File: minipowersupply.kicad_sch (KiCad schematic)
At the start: 43 parts, among them J1 Conn_01x08_Female, J2 Conn_01x08_Female, J3 Conn_01x03_Female, J4 Conn_01x08_Female, J5 Conn_01x03_Female, J6 Conn_01x08_Female, J7 Conn_01x03_Female, J8 Conn_01x02_Female, J9 Conn_01x02_Female, Q1 BC817, U1 LM7805_TO220, U15 LT1084-3.3, U2 LM317L_TO92, U3 LM337L_TO92, U4 CD74HC4067SM

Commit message: finalising diagram
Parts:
- removed A1: Arduino_Nano_v2.x, Module:Arduino_Nano, symbol MCU_Module:Arduino_Nano_v2.x
- removed C1, C2: 150uF, Capacitor_THT:CP_Radial_D8.0mm_P3.50mm, symbol minipowersupply-rescue:CP-Device
- removed C3, C4, C5, C6, C8: 100nF, Capacitor_THT:C_Disc_D8.0mm_W5.0mm_P5.00mm, symbol Device:C
- removed C7, C9: 1uF, Capacitor_THT:C_Disc_D8.0mm_W5.0mm_P5.00mm, symbol Device:C_Polarized_Small
- removed D1, D2, D3, D4, D5, D6: D, Diode_THT:D_T-1_P10.16mm_Horizontal, symbol Device:D
- removed F1: Fuse, Fuse:Fuseholder_Cylinder-5x20mm_Bulgin_FX0457_Horizontal_Closed, symbol Device:Fuse
- removed J1, J2, J4, J6: Conn_01x08_Female, Connector_PinHeader_2.54mm:PinHeader_1x08_P2.54mm_Vertical, symbol Connector:Conn_01x08_Female
- removed J3, J5, J7: Conn_01x03_Female, Connector_PinHeader_2.54mm:PinHeader_1x03_P2.54mm_Vertical, symbol Connector:Conn_01x03_Female
- removed J8, J9: Conn_01x02_Female, Connector_PinHeader_2.54mm:PinHeader_1x02_P2.54mm_Vertical, symbol Connector:Conn_01x02_Female
- removed Q1: BC817, Package_TO_SOT_SMD:SOT-23, symbol Transistor_BJT:BC817
- removed R1: 410, Resistor_THT:R_Axial_DIN0207_L6.3mm_D2.5mm_P5.08mm_Vertical, symbol Device:R_Small
- removed R2: 4.420k, Resistor_THT:R_Axial_DIN0207_L6.3mm_D2.5mm_P5.08mm_Vertical, symbol Device:R_Small
- removed R3: 698, Resistor_THT:R_Axial_DIN0207_L6.3mm_D2.5mm_P5.08mm_Vertical, symbol Device:R_Small
- removed R4, R5: 240, Resistor_THT:R_Axial_DIN0207_L6.3mm_D2.5mm_P5.08mm_Vertical, symbol Device:R_Small
- removed RV1, RV2: 5k, symbol minipowersupply-rescue:R_POT_Small-Device
- removed TP1, TP2, TP3: TestPoint, TestPoint:TestPoint_THTPad_4.0x4.0mm_Drill2.0mm, symbol Connector:TestPoint
- removed TR1: TRANSF3, minipowersupply:vtxtfr, symbol Transformer:TRANSF3
- removed U1: LM7805_TO220, Package_TO_SOT_SMD:SOT-223-3_TabPin2, symbol Regulator_Linear:LM7805_TO220
- removed U15: LT1084-3.3, symbol Regulator_Linear:LT1084-3.3
- removed U2: LM317L_TO92, Package_TO_SOT_THT:TO-92_Inline, symbol Regulator_Linear:LM317L_TO92
- removed U3: LM337L_TO92, Package_TO_SOT_THT:TO-92_Inline, symbol Regulator_Linear:LM337L_TO92
- removed U4: CD74HC4067SM, Package_SO:SSOP-24_5.3x8.2mm_P0.65mm, symbol 74xx:CD74HC4067SM
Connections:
- no-connect marks 31 -> 1
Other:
- removed sheet Curent and Volt4
- removed sheet Curent and Volt5
- removed sheet Curent and Volt6
- removed sheet Curent and Volt7
- removed sheet Curent and Volt8
- added sheet  Measure and Mux (arduino.kicad_sch)
- added sheet Clock and TTL (CKTTL.kicad_sch)
- added sheet DualAdj (dualadj.kicad_sch)
- added sheet Measure and Control (MAC.kicad_sch)
- added sheet Unregulated Power (untitled.kicad_sch)
- note removed: "Adjustable Dual Regulated Supply"
- note removed: "Clock Pulse Generator"
- note removed: "Dual Adjustable Regulated Supply"
- note removed: "Low Voltage"
- note removed: "Mains"
- note removed: "Outputs"
- note removed: "Regulated Power"
- note removed: "Regulated TTL and 100Hz CK"
- note removed: "Unregulated Dual Supply"
- note removed: "Unregulated Power"

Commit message: last TH mounting board
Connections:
- no-connect marks 1 -> 0
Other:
- sheet Measure and Control ports: added GND; removed none
- sheet Unregulated Power: file untitled.kicad_sch -> Unregpower.kicad_sch

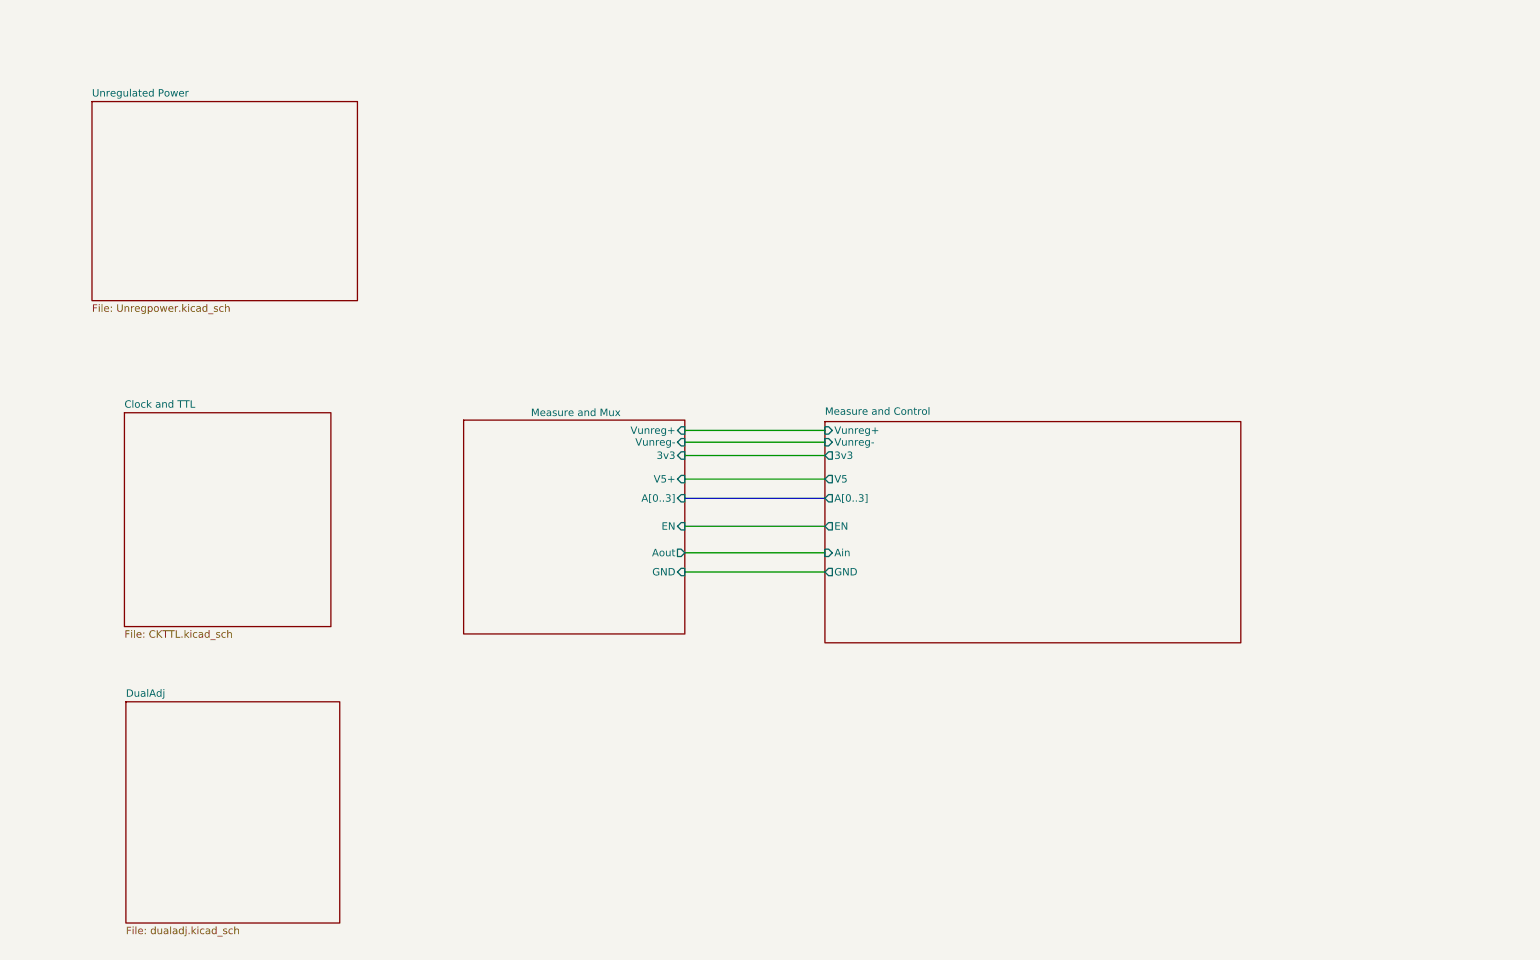
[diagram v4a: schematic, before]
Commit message: new board with SMD
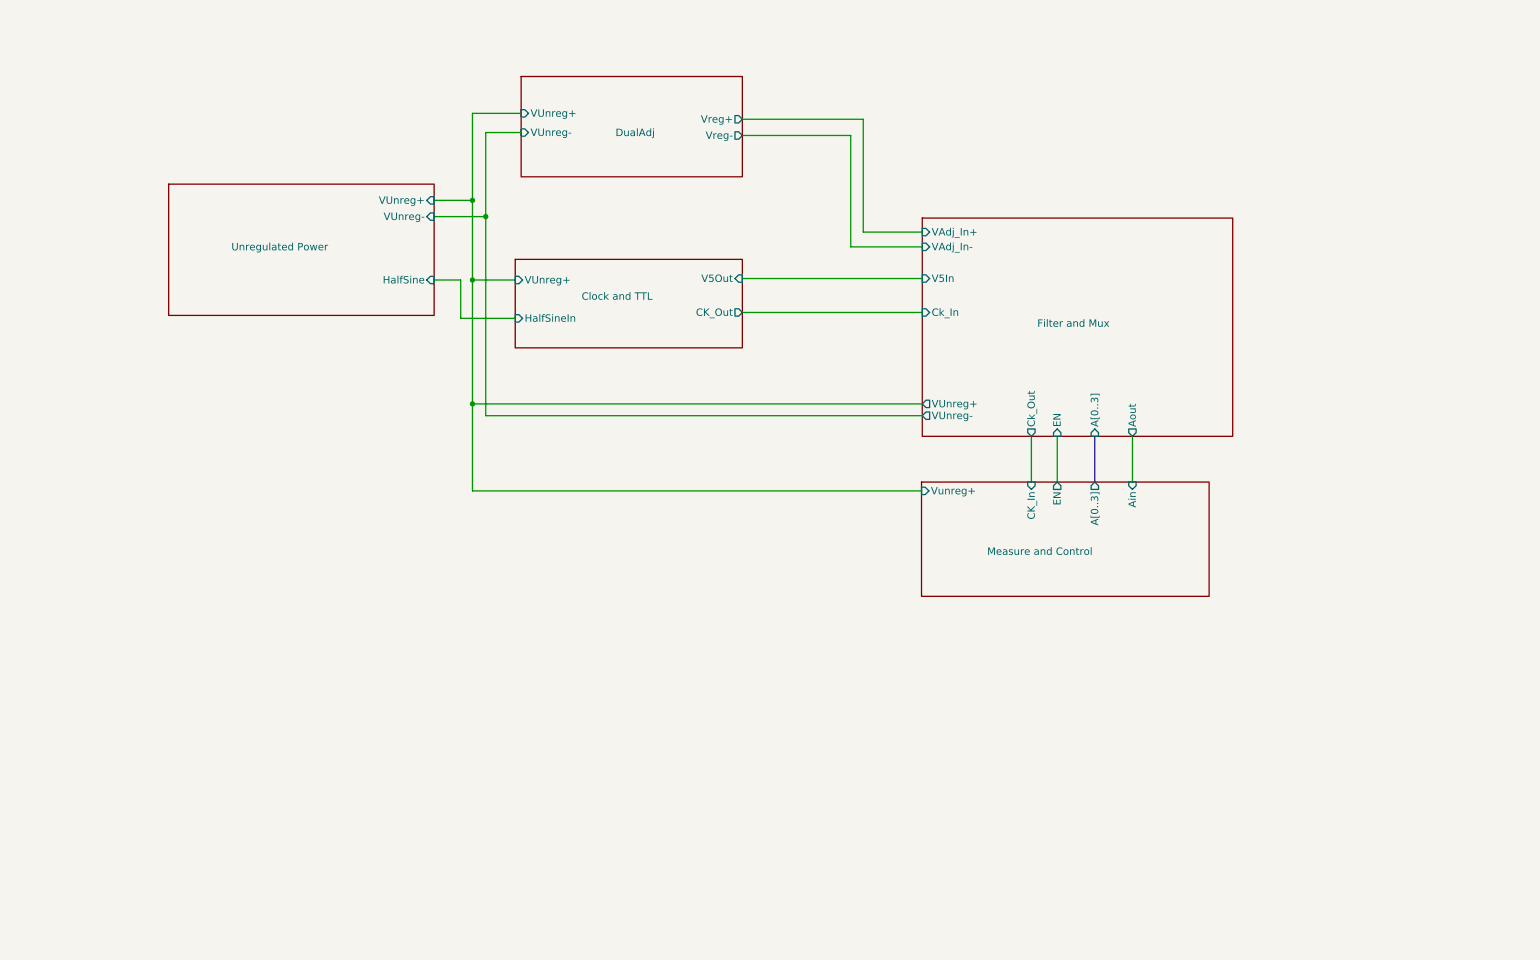
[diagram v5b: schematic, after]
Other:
- sheet  Measure and Mux renamed Filter and Mux
- sheet Clock and TTL ports: added CK_Out, HalfSineIn, V5Out, VUnreg+; removed none
- sheet DualAdj ports: added VUnreg+, VUnreg-, Vreg+, Vreg-; removed none
- sheet Filter and Mux ports: added Ck_In, Ck_Out, V5In, VAdj_In+, VAdj_In-, VUnreg+, VUnreg-; removed 3v3, GND, V5+, Vunreg+, Vunreg-
- sheet Measure and Control ports: added CK_In; removed 3v3, GND, V5, Vunreg-
- sheet Unregulated Power ports: added HalfSine, VUnreg+, VUnreg-; removed none

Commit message: New single board with all SMD in progress
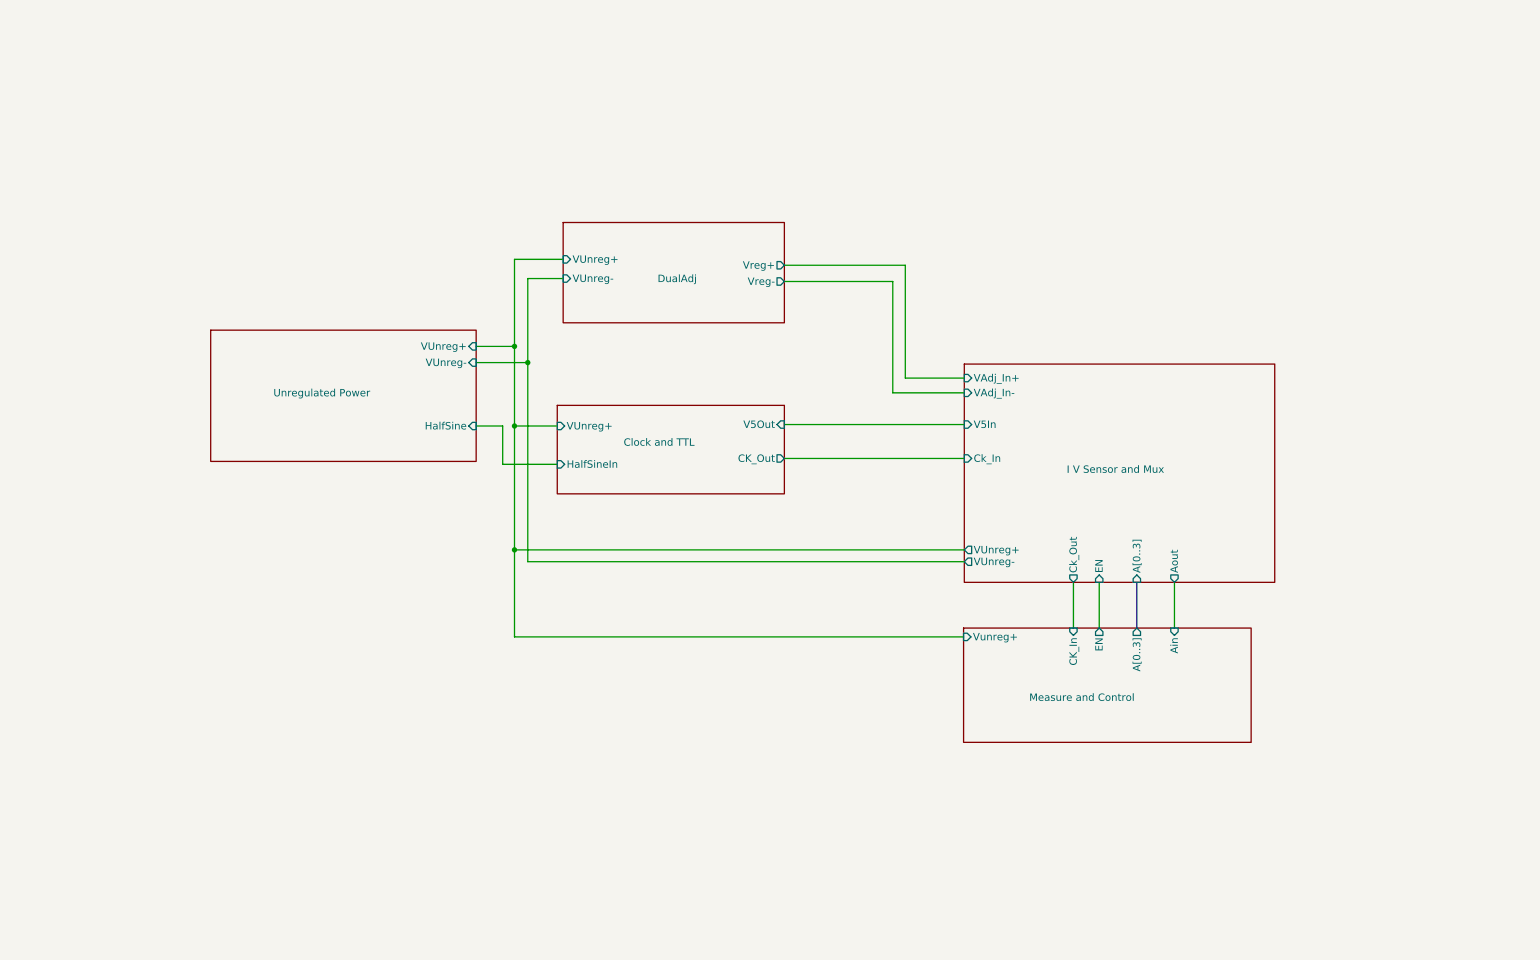
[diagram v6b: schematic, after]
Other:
- sheet Filter and Mux renamed I V Sensor and Mux

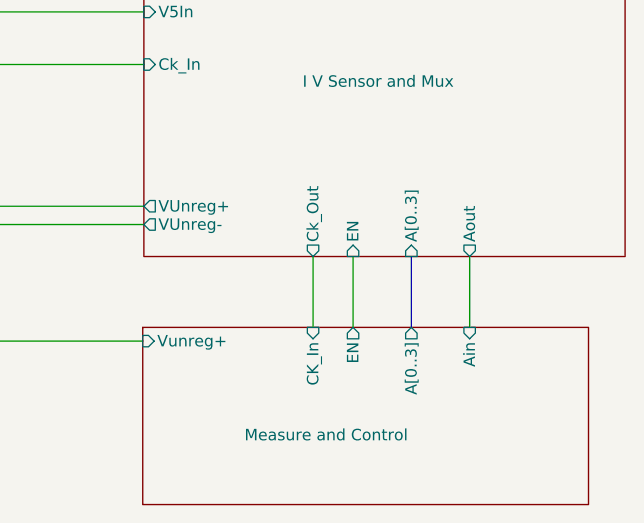
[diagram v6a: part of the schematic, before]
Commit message: Updated improved board for all SMD
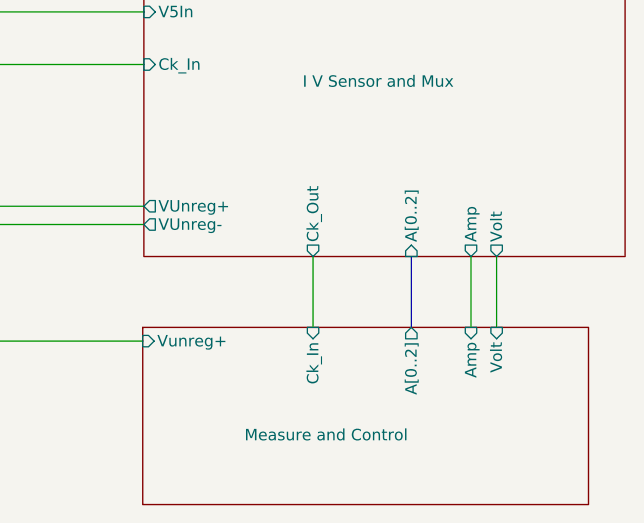
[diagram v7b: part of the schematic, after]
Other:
- sheet I V Sensor and Mux ports: added A[0..2], Amp, Volt; removed A[0..3], Aout, EN
- sheet Measure and Control ports: added A[0..2], Amp, Ck_In, Volt; removed A[0..3], Ain, CK_In, EN
